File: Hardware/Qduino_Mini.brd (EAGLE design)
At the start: 20.3 x 38.1 mm, 41 parts, among them Q1 PFET, U1 ATMEGA32U41:1-LESS_PASTE, U2 MCP73831, U3 MAX17048, U4 AP2112K-3.3TRG-1, U5 MIGHTYQ-L-SILK, Y1 8MHZ

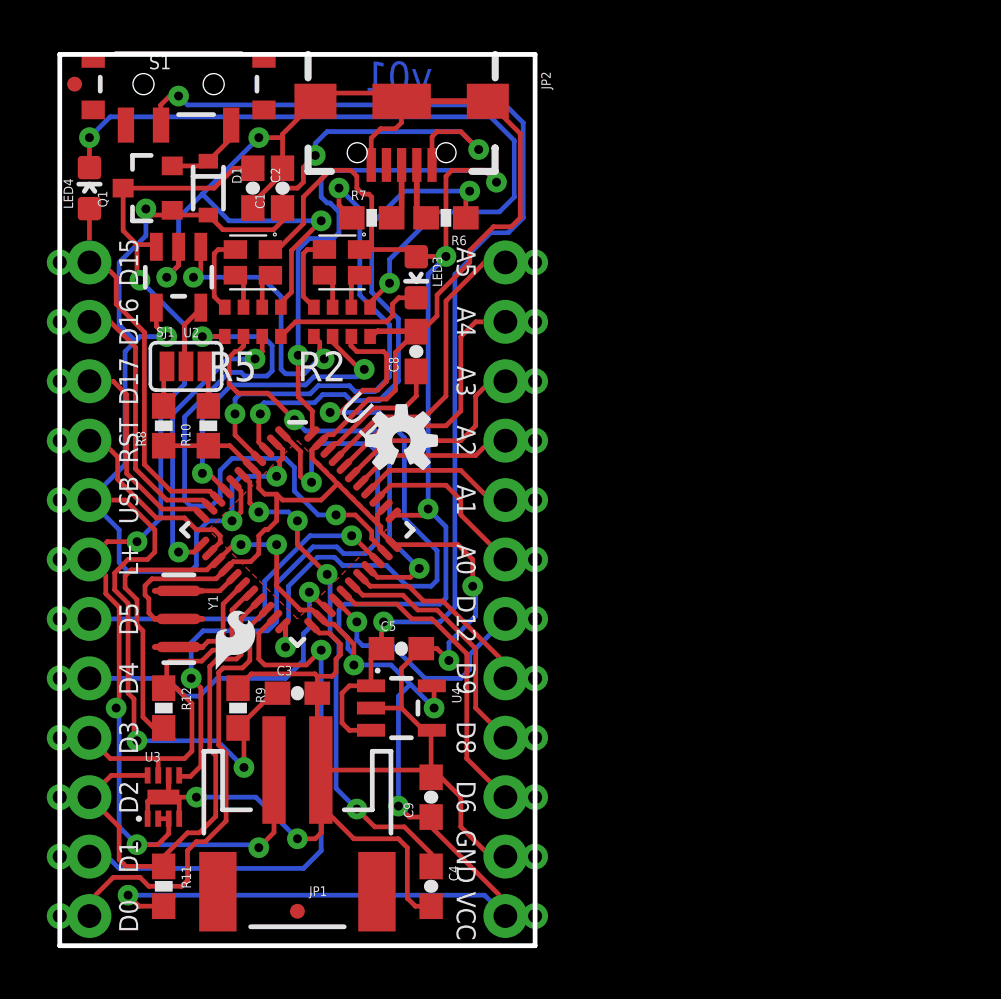
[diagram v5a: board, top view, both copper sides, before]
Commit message: Renamed a few parts and removed gnd traces under gnd pours
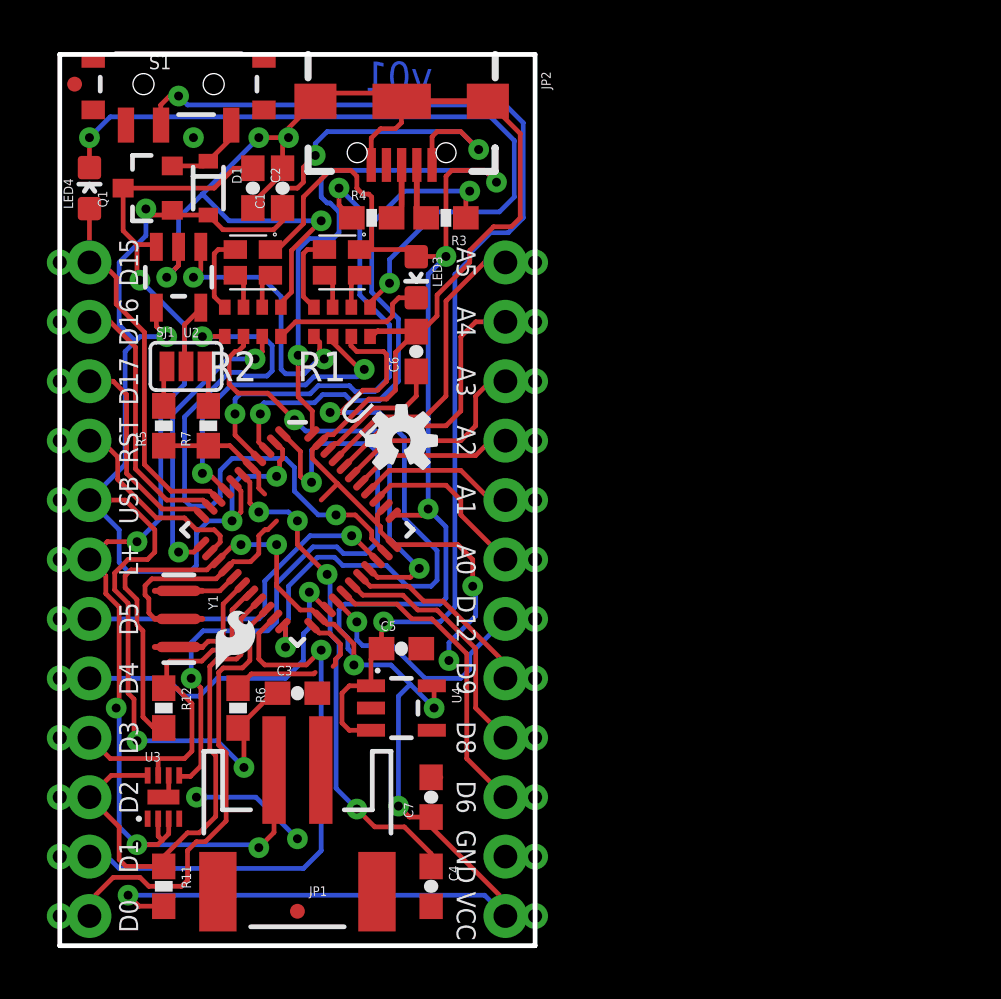
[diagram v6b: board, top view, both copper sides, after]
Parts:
- removed R10: 10K, SparkFun-Resistors:0603-RES
- removed R8: 2.0k, SparkFun-Resistors:0603-RES
- removed R9: 100k, SparkFun-Resistors:0603-RES
- added R1: 330, SparkFun-Passives:0603-ARV
- added R3, R4: 22, SparkFun-Resistors:0603-RES
- R5: value 330 -> 2.0k; device SparkFun-Passives:0603-ARV -> SparkFun-Resistors:0603-RES
- R6: value 22 -> 100k
- R7: value 22 -> 10K
- moved R6 22.8 mm to (7.62, 10.2), turned to 270 degrees
- moved R7 11.3 mm to (6.35, 22.2), turned to 90 degrees
- moved R5 5.85 mm to (4.45, 22.2), turned to 90 degrees
- moved R2 3.81 mm to (8.26, 26.7)
- renumbered C8 to C6, C9 to C7
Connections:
- net D+: now also R4.1; no longer R7.1
- net D-: now also R3.1; no longer R6.1
- net D10: now also R2.2; no longer R5.2
- net D11: now also R2.3; no longer R5.3
- net D13: now also R2.1; no longer R5.1
- net GND: now also R1.4, R2.5, R5.1, R6.1, R7.1; no longer R10.1, R2.4, R5.5, R8.1, R9.1
- net N$1: now also R1.8; no longer R2.8
- net N$2: now also R1.6; no longer R2.6
- net N$32: now also R2.6; no longer R5.6
- net N$34: now also R1.7; no longer R2.7
- net N$35: now also R2.8; no longer R5.8
- net N$37: now also R2.7; no longer R5.7
- net N$4: now also R2.4; no longer R5.4
- net N$5: now also R1.5; no longer R2.5
- net N$6: now also R7.2; no longer R10.2
- net N$7: now also R5.2; no longer R8.2
- net RXLED: now also R1.3; no longer R2.3
- net STAT: now also R1.1; no longer R2.1
- net TXLED: now also R1.2; no longer R2.2
- net UD+: now also R4.2; no longer R7.2
- net UD-: now also R3.2; no longer R6.2
- net VBUS: now also R6.2; no longer R9.2
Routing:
- net GND: track 151.1 -> 108.4 mm, vias 8 -> 10
- net LIPO: track 52.1 -> 52.6 mm
- removed copper zone on layer 1, net N$3

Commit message: Converted more parts to parts SFE uses
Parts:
- removed JP1: LiPo, SparkFun:JST-2-SMD
- added J1: LiPo, SparkFun-Connectors:JST-2-SMD
- D1: value 250mA/100V -> BAT20J
- moved FID2 4.90 mm to (5.33, 0.64)
- renumbered LED1 to D2, LED2 to D3, LED3 to D4, LED4 to D5
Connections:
- net GND: now also J1.1; no longer JP1.1
- net LIPO: now also J1.2; no longer JP1.2
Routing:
- net GND: track 108.4 -> 106.6 mm
